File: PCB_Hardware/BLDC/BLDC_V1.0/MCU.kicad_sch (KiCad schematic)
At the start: 15 parts, among them J7 Conn_ARM_JTAG_SWD_10, U7 STM32G474RET6, Y2 XXGBBCNANF-25.000000MHZ

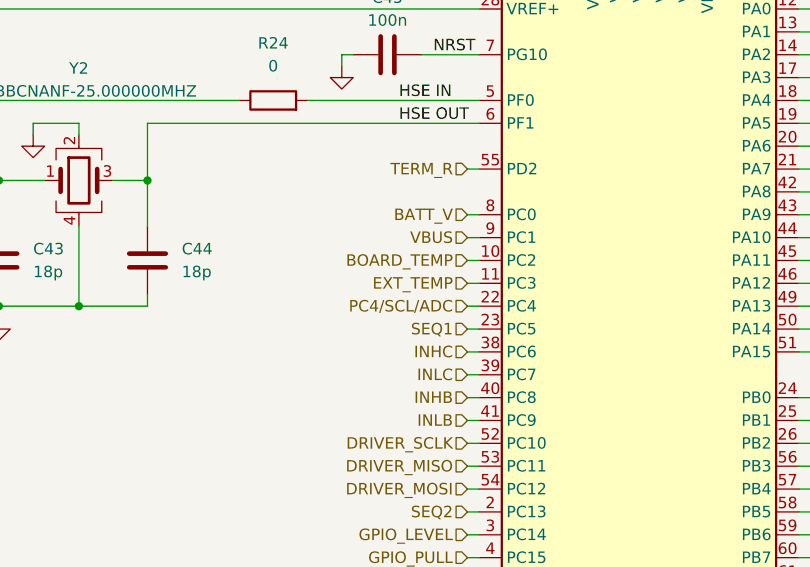
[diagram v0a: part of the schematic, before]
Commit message: Removed external temp sensing bc I forgot the calibration enable pin for the encoder
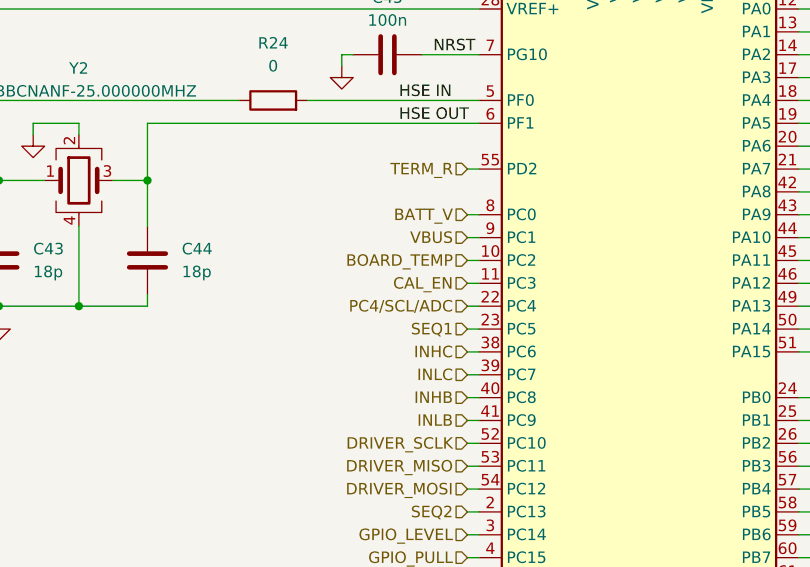
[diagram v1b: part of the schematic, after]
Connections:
- net EXT_TEMP renamed CAL_EN

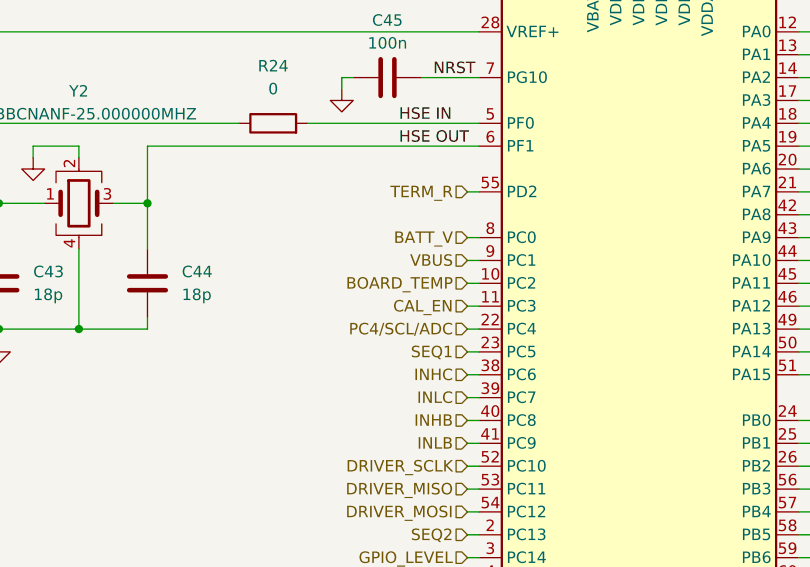
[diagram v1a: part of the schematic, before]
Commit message: redid external temp sensing and instead removed V Bus sense from the USBC input
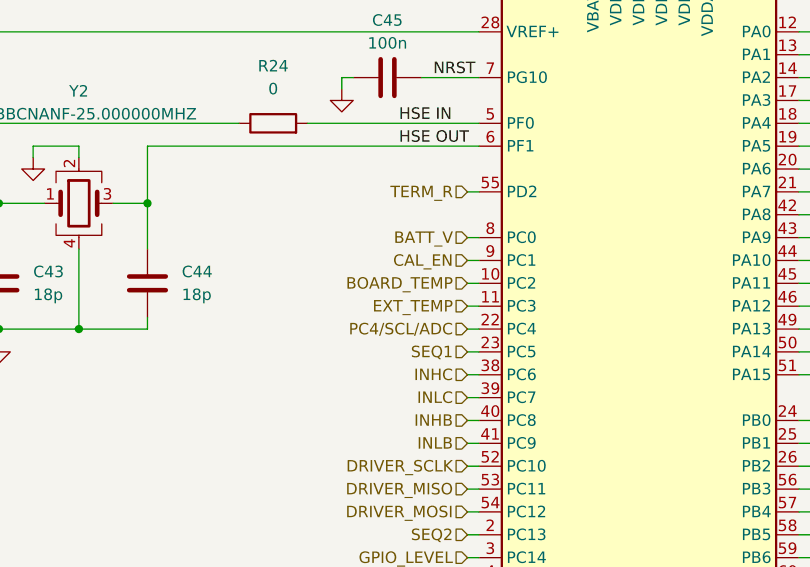
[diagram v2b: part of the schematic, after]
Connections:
- net VBUS is gone; now on net CAL_EN: U7.9 (PC1)
- net CAL_EN: no longer U7.11 (PC3)
- new net EXT_TEMP: U7.11 (PC3)

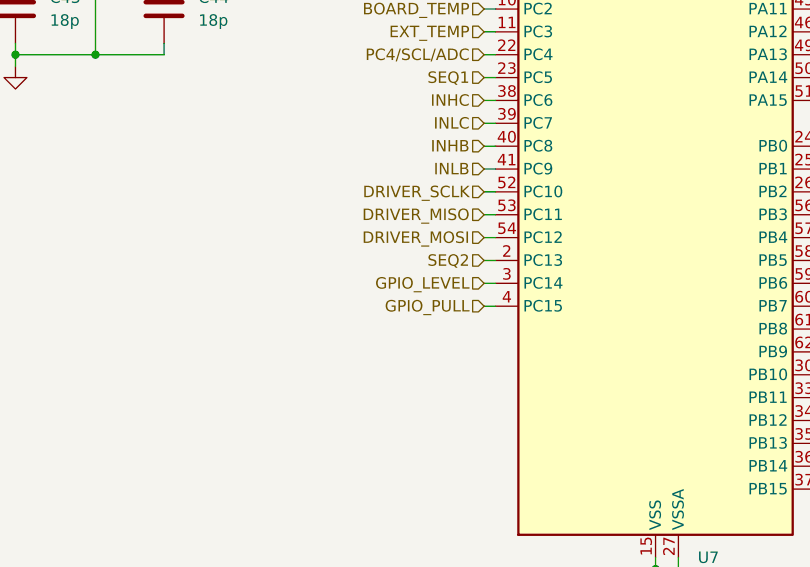
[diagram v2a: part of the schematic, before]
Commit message: foget to add the GPIO to change the voltage for AUX2 SPI port, removed the ability to pull AUX pins down to free a pin
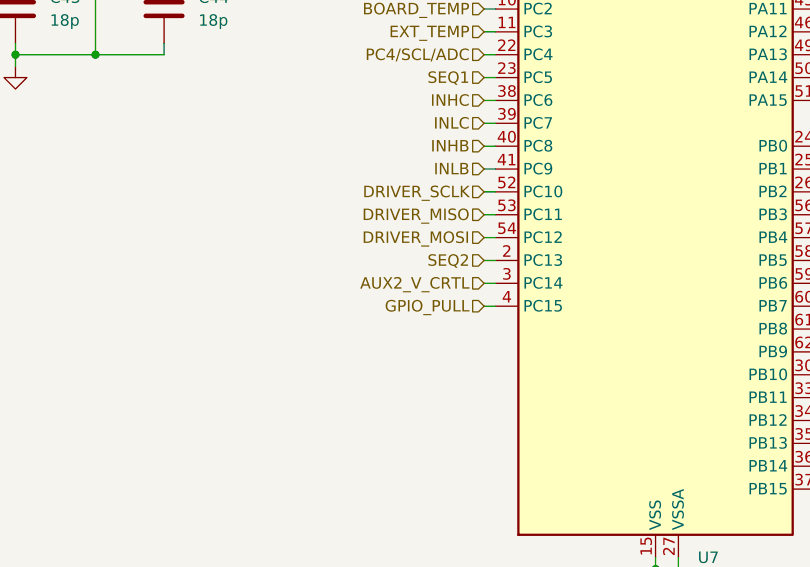
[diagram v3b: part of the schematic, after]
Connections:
- net GPIO_LEVEL renamed AUX2_V_CRTL
